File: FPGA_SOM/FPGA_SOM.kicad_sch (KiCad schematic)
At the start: 64 parts, among them J1 Conn_01x14, J2 Conn_01x09, J3 Conn_01x11, J4 Conn_01x04, J5 Conn_01x02, J6 Conn_02x04_Counter_Clockwise, U1 ICE40UP5K-SG48ITR, U101 W25X20CLSN, U2 AP2127N-3.3, U3 AP2127N-1.2, X101 ECS-2520MV-xxx-xx

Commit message: Saving progress.
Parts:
- removed D1: 1N4004, Diode_SMD:D_0603_1608Metric, symbol Diode:1N4004
- removed D102: LED, Diode_SMD:D_0603_1608Metric, symbol Device:LED
- removed J1: Conn_01x14, Connector_PinHeader_2.54mm:PinHeader_1x14_P2.54mm_Vertical, symbol Connector_Generic:Conn_01x14
- removed J2: Conn_01x09, Connector_PinHeader_2.54mm:PinHeader_1x09_P2.54mm_Vertical, symbol Connector_Generic:Conn_01x09
- removed J3: Conn_01x11, Connector_PinHeader_2.54mm:PinHeader_1x11_P2.54mm_Vertical, symbol Connector_Generic:Conn_01x11
- removed J4: Conn_01x04, Connector_PinHeader_2.54mm:PinHeader_1x04_P2.54mm_Vertical, symbol Connector_Generic:Conn_01x04
- removed J6: Conn_02x04_Counter_Clockwise, Connector_PinHeader_2.54mm:PinHeader_2x04_P2.54mm_Vertical, symbol Connector_Generic:Conn_02x04_Counter_Clockwise
- removed R102: 10k, Resistor_SMD:R_0603_1608Metric, symbol Device:R
- removed R103 (x2): 0, Resistor_SMD:R_0603_1608Metric, symbol Device:R
- removed R111, R3, R4, R5: 1k, Resistor_SMD:R_0603_1608Metric, symbol Device:R
- removed TP2: TestPoint, TestPoint:TestPoint_Pad_2.0x2.0mm, symbol Connector:TestPoint
- added H1, H2, H3, H4: MountingHole, MountingHole:MountingHole_3.2mm_M3, symbol Mechanical:MountingHole
- added J1: Conn_01x12, Connector_PinHeader_2.54mm:PinHeader_1x12_P2.54mm_Vertical, symbol Connector_Generic:Conn_01x12
- added J2: Conn_02x05_Counter_Clockwise, Connector_PinHeader_2.54mm:PinHeader_2x05_P2.54mm_Vertical, symbol Connector_Generic:Conn_02x05_Counter_Clockwise
- added J3: Conn_01x06, Connector_PinHeader_2.54mm:PinHeader_1x06_P2.54mm_Vertical, symbol Connector_Generic:Conn_01x06
- added J7: Conn_01x09, Connector_PinHeader_2.54mm:PinHeader_1x09_P2.54mm_Vertical, symbol Connector_Generic:Conn_01x09
- added J8: Conn_01x10, Connector_PinHeader_2.54mm:PinHeader_1x10_P2.54mm_Vertical, symbol Connector_Generic:Conn_01x10
- added R102 (x2), R103 (x2): 10k, Resistor_SMD:R_0603_1608Metric, symbol Device:R
- added R103 (x2): 0, Resistor_SMD:R_0603_1608Metric, symbol Device:R
- C122: value 10u -> 4.7u; footprint Capacitor_SMD:C_0805_2012Metric -> Capacitor_SMD:C_0603_1608Metric
- C137: value 22u -> 10u
- TP1: value TestPoint -> VPLL
- TP10: value TestPoint -> ~{RST}
- TP11: value TestPoint -> CDN
- TP12: value TestPoint -> OSC
- TP3: value TestPoint -> 3V3
- TP4: value TestPoint -> 1V2
- TP5: value TestPoint -> FSS
- TP6: value TestPoint -> ISS
- TP7: value TestPoint -> SCK
- TP8: value TestPoint -> SDO
- TP9: value TestPoint -> SDI
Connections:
- net +5V: now also J1.12 (Pin_12)
- net 3V3: now also U1.24 (VPP_2V5), J1.11 (Pin_11), J2.8 (Pin_8), R102.1, R102.1, R103.1, R103.1
- net CDONE: now also J2.9 (Pin_9), J8.5 (Pin_5)
- net CRESET: now also J2.10 (Pin_10), J8.6 (Pin_6), R102.2
- net FLASH_SS: now also J2.1 (Pin_1)
- net GND: now also J1.10 (Pin_10), J2.7 (Pin_7)
- net ICE_SS: now also R103.2
- net SCK: now also J2.4 (Pin_4), R103.2
- net VCCPLL: now also TP1.1
- net RGB0: now reaches D2.1 (K)
- net RGB0: now also U1.39 (RGB0)
- net V_OSC: now reaches C134.1, C138.1, C143.2, FB1.2, X101.1 (Tri-State), X101.4 (VDD)
- net 20: now reaches U1.20 (IOB_25b_G3)
- net 20: now also J3.4 (Pin_4)
- net 21: now reaches U1.21 (IOB_23b)
- net 21: now also J3.5 (Pin_5)
- net 6: now reaches U1.6 (IOB_13b)
- net 6: now also J8.4 (Pin_4)
- net 9: now reaches U1.9 (IOB_16a)
- net 9: now also J8.7 (Pin_7)
- net 10: now reaches U1.10 (IOB_18a)
- net 10: now also J8.8 (Pin_8)
- net 11: now reaches U1.11 (IOB_20a)
- net 11: now also J8.9 (Pin_9)
- net 12: now reaches U1.12 (IOB_22a)
- net 12: now also J8.10 (Pin_10)
- net 13: now reaches U1.13 (IOB_24a)
- net 13: now also J3.1 (Pin_1)
- net 18: now reaches U1.18 (IOB_31b)
- net 18: now also J3.2 (Pin_2)
- net 19: now reaches U1.19 (IOB_29b)
- net 19: now also J3.3 (Pin_3)
- net RGB2: now reaches D4.1 (K)
- net RGB2: now also U1.41 (RGB2)
- net 23: now reaches U1.23 (IOT_37a)
- net 23: now also J3.6 (Pin_6)
- net 25: now reaches U1.25 (IOT_36b)
- net 25: now also J7.1 (Pin_1)
- net 26: now reaches U1.26 (IOT_39a)
- net 26: now also J7.2 (Pin_2)
- net 27: now reaches U1.27 (IOT_38b)
- net 27: now also J7.3 (Pin_3)
- net 28: now reaches U1.28 (IOT_41a)
- net 28: now also J7.4 (Pin_4)
- net RDP_N: now reaches U1.31 (IOT_42b)
- net RDP_N: now also J7.5 (Pin_5)
- net RDP_P: now reaches U1.32 (IOT_43a)
- net RDP_P: now also J7.6 (Pin_6)
- net 34: now reaches U1.34 (IOT_44b)
- net 34: now also J7.7 (Pin_7)
- net 35_G0: now reaches U1.35 (IOT_46b_G0)
- net 35_G0: now also J7.8 (Pin_8)
- net 36: now reaches U1.36 (IOT_48b)
- net 36: now also J7.9 (Pin_9)
- net 37_G1: now reaches U1.37 (IOT_45a_G1)
- net 37_G1: now also J1.1 (Pin_1)
- net 38: now reaches U1.38 (IOT_50b)
- net 38: now also J1.2 (Pin_2)
- net RGB1: now reaches U1.40 (RGB1)
- net RGB1: now also D3.1 (K)
- net 42: now reaches U1.42 (IOT_51a)
- net 42: now also J1.3 (Pin_3)
- net 43: now reaches U1.43 (IOT_49a)
- net 43: now also J1.4 (Pin_4)
- net 45: now reaches U1.45 (IOB_5b)
- net 45: now also J1.6 (Pin_6)
- net DP1_N: now reaches U1.46 (IOB_0a)
- net DP1_N: now also J1.7 (Pin_7)
- net DP1_P: now reaches U1.47 (IOB_2a)
- net DP1_P: now also J1.8 (Pin_8)
- net 48: now reaches U1.48 (IOB_4a)
- net 48: now also J1.9 (Pin_9)
- net 2: now reaches U1.2 (IOB_6a)
- net 2: now also J8.1 (Pin_1)
- net 3: now reaches U1.3 (IOB_9b)
- net 3: now also J8.2 (Pin_2)
- net 4: now reaches U1.4 (IOB_8a)
- net 4: now also J8.3 (Pin_3)
- net at R102.2, U101.3 (~{WP}): no longer U101.7 (~{HOLD})
- net FLASH_MISO renamed FLASH_DO
- net FLASH_DO: now also J2.2 (Pin_2), R103.1; no longer U1.17 (IOB_33b_SPI_SI)
- net FLASH_MOSI renamed FLASH_DI
- net FLASH_DI: now also J2.3 (Pin_3), R103.1; no longer U1.14 (IOB_32a_SPI_SO)
- net FPGA_OSCILLATOR renamed CLK_IN_G6
- net CLK_IN_G6: now also J1.5 (Pin_5)
- new net: R103.2, U1.17 (IOB_33b_SPI_SI)
- new net: R103.2, U1.14 (IOB_32a_SPI_SO)
- new net: R102.2, U101.7 (~{HOLD})
- no-connect marks 0 -> 2
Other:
- note added: "10-pin IDC Programming Header"
- note added: "1V2 Power supply"
- note added: "3V3 Power supply"
- note added: "Bottom Header"
- note added: "CMOS Crystal oscillator 50 MHz"
- note added: "Don't need resistors as FPGA has programmable current sinks"
- note added: "FPGA Banks and CDONE Indicator LED"
- note added: "Idea of header locations"
- note added: "Left Header"
- note added: "Mounting holes"
- note added: "Non-IO FPGA Power Only need 2.5V if programming NVCM"
- note added: "Pin 30"
- note added: "Pin 5"
- note added: "Right Header"
- note added: "Top Header"
- note added: "VPLL Filtering"
- note added: "between flash and FPGA"
- note added: "between input and flash"
- note removed: "3V3 FPGA decoupling capacitors"
- note removed: "Crystal oscillator for FPGA"
- note removed: "Power supply 3V3, 1V2 and PLL power supply filter"
- note removed: "SPI and I2C pins are not preassigned. I3C pins are:"
- moved on the sheet: C101, C104, C119, C122, C125, C126, C131, C133, C134, C137, C138, C143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

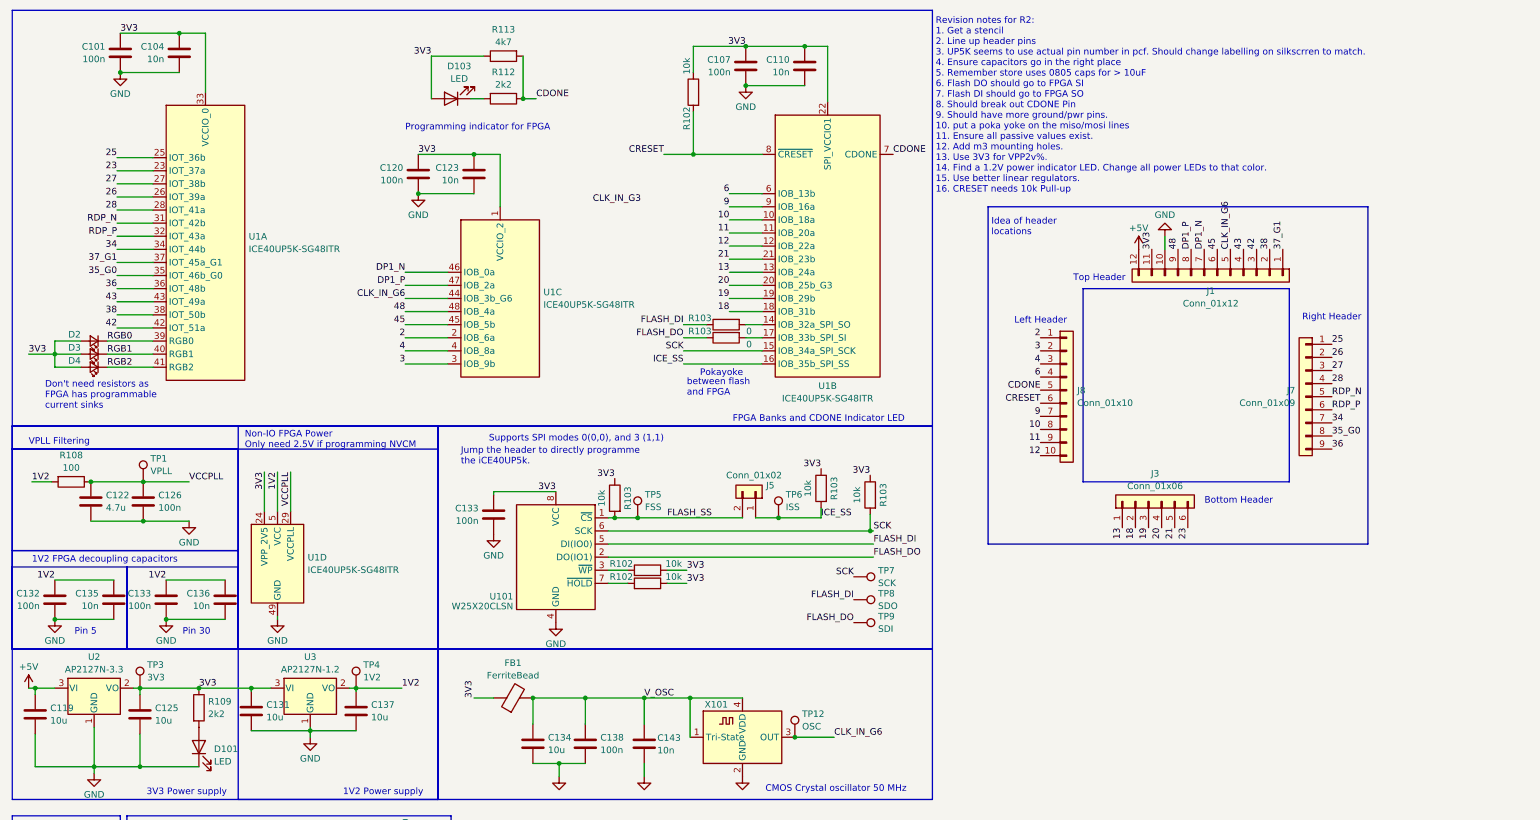
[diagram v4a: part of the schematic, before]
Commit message: Remove some unnecessary capacitors and resize others.
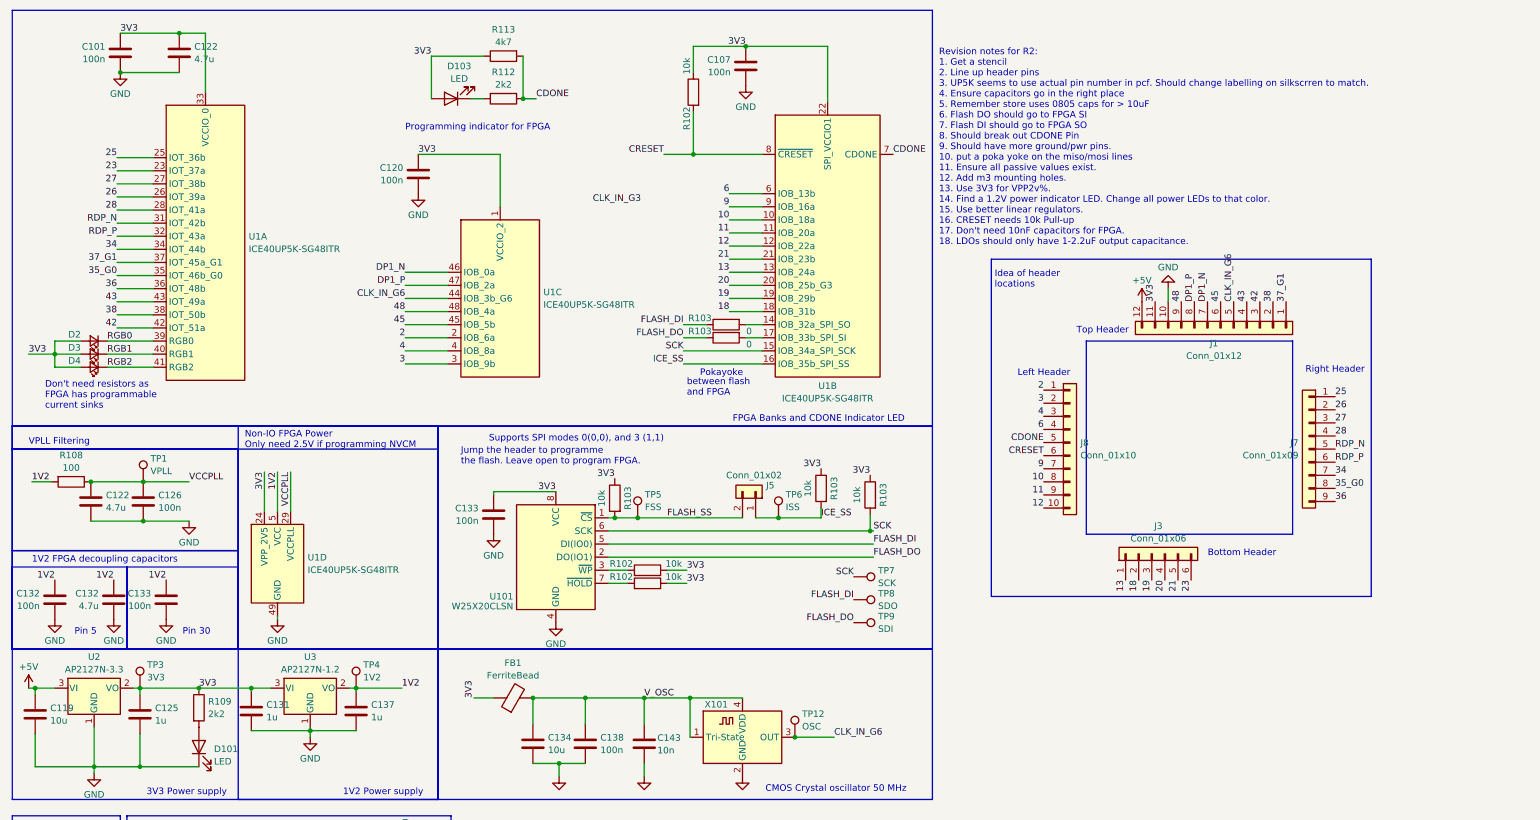
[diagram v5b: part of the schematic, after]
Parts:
- removed C104, C110, C123, C135, C136: 10n, Capacitor_SMD:C_0603_1608Metric, symbol Device:C
- added C122, C132: 4.7u, Capacitor_SMD:C_0603_1608Metric, symbol Device:C
- C125, C131, C137: value 10u -> 1u; footprint Capacitor_SMD:C_0805_2012Metric -> Capacitor_SMD:C_0603_1608Metric
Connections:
- net 1V2: now also C132.1
- net 3V3: now also C122.1
- net GND: now also C122.2, C132.2
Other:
- note added: "Jump the header to programme the flash. Leave open to program FPGA."
- note removed: "Jump the header to directly programme the iCE40UP5k."
- moved on the sheet: J1, J3, J7, J8

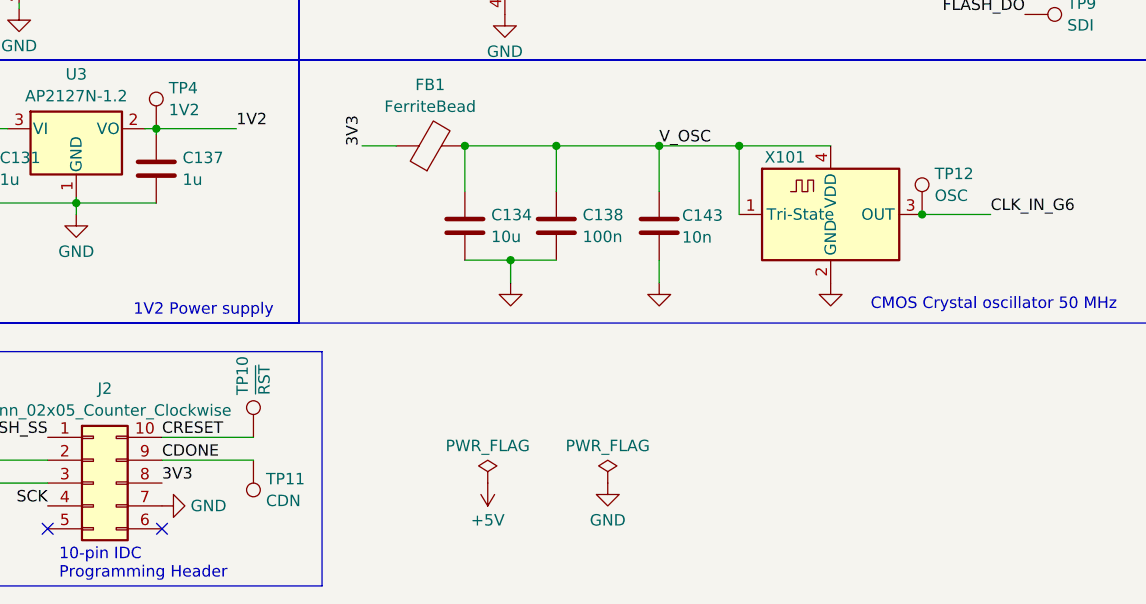
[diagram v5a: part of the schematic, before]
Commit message: Added silkscreen and removed unneded test points.
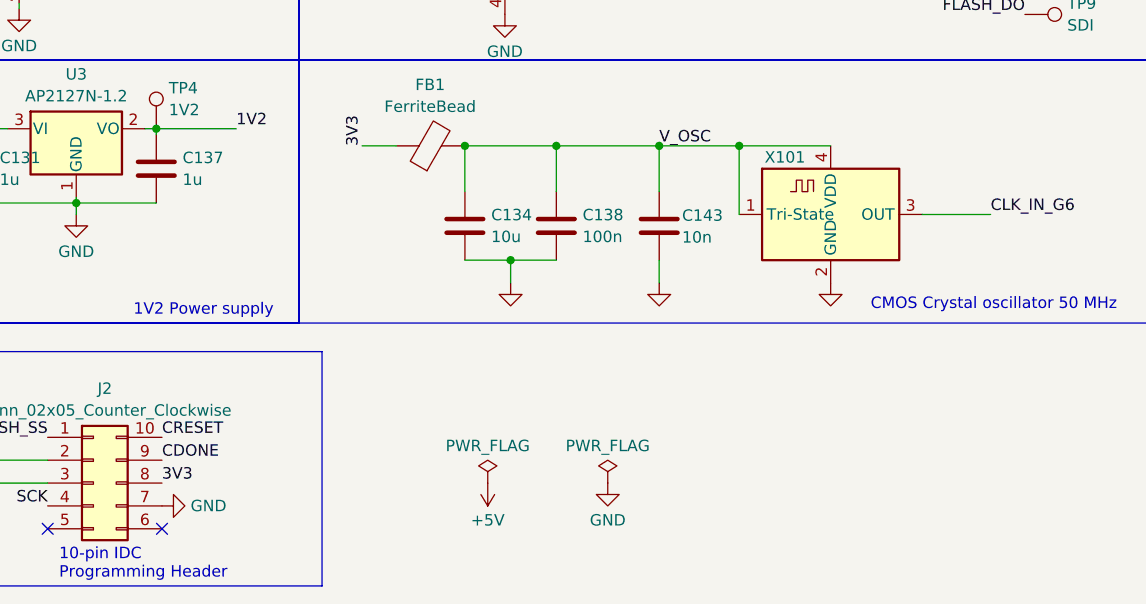
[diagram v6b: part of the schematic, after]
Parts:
- removed TP10: ~{RST}, TestPoint:TestPoint_Pad_2.0x2.0mm, symbol Connector:TestPoint
- removed TP11: CDN, TestPoint:TestPoint_Pad_2.0x2.0mm, symbol Connector:TestPoint
- removed TP12: OSC, TestPoint:TestPoint_Pad_2.0x2.0mm, symbol Connector:TestPoint
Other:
- company: (none) -> Tobias McKellar
- title: (none) -> FPGA System on Module
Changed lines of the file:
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@@
 (kicad_sch (version 20230121) (generator eeschema)
   (paper "A4")
+  (title_block
+    (title "FPGA System on Module")
+    (rev "2")
+    (company "Tobias McKellar")
+  )
   (junction (at 38.735 104.14) (diameter 0) (color 0 0 0 0)
   )
@@
   )
   (junction (at 130.175 111.125) (diameter 0) (color 0 0 0 0)
-  )
-  (junction (at 165.1 153.67) (diameter 0) (color 0 0 0 0)
   )
   (junction (at 38.735 111.76) (diameter 0) (color 0 0 0 0)
@@
     (stroke (width 0) (type default))
   )
-  (wire (pts (xy 90.805 180.975) (xy 80.645 180.975))
-    (stroke (width 0) (type default))
-  )
   (wire (pts (xy 33.655 53.975) (xy 40.64 53.975))
     (stroke (width 0) (type default))
@@
   )
   (wire (pts (xy 143.51 73.66) (xy 147.955 73.66))
-    (stroke (width 0) (type default))
-  )
-  (wire (pts (xy 90.805 178.435) (xy 80.645 178.435))
     (stroke (width 0) (type default))
   )
@@
     )
   )
-  (symbol (lib_id "Connector:TestPoint") (at 90.805 178.435 0) (unit 1)
-    (in_bom yes) (on_board yes) (dnp no)
-    (property "Reference" "TP10" (at 89.5929 173.736 90)
-      (effects (font (size 1.27 1.27)) (justify left))
-    )
-    (property "Value" "~{RST}" (at 92.0171 173.736 90)
-      (effects (font (size 1.27 1.27)) (justify left))
-    )
-    (property "Footprint" "TestPoint:TestPoint_Pad_2.0x2.0mm" (at 95.885 178.435 0)
-      (effects (font (size 1.27 1.27)) hide)
-    )
-    (property "Datasheet" "~" (at 95.885 178.435 0)
-      (effects (font (size 1.27 1.27)) hide)
-    )
-    (pin "1")
-    (instances
-      (project "FPGA_SOM"
-        (path "/c9513ae4-ec90-4b73-ae24-d135d02c4e68"
-          (reference "TP10") (unit 1)
-        )
-      )
-    )
-  )
   (symbol (lib_id "Connector:TestPoint") (at 176.53 131.445 270) (unit 1)
     (in_bom yes) (on_board yes) (dnp no) (fields_autoplaced)
@@
     )
   )
-  (symbol (lib_id "Connector:TestPoint") (at 165.1 153.67 0) (unit 1)
-    (in_bom yes) (on_board yes) (dnp no) (fields_autoplaced)
-    (property "Reference" "TP12" (at 166.497 149.1559 0)
-      (effects (font (size 1.27 1.27)) (justify left))
-    )
-    (property "Value" "OSC" (at 166.497 151.5801 0)
-      (effects (font (size 1.27 1.27)) (justify left))
-    )
-    (property "Footprint" "TestPoint:TestPoint_Pad_2.0x2.0mm" (at 170.18 153.67 0)
-      (effects (font (size 1.27 1.27)) hide)
-    )
-    (property "Datasheet" "~" (at 170.18 153.67 0)
-      (effects (font (size 1.27 1.27)) hide)
-    )
-    (pin "1")
-    (instances
-      (project "FPGA_SOM"
-        (path "/c9513ae4-ec90-4b73-ae24-d135d02c4e68"
-          (reference "TP12") (unit 1)
-        )
-      )
-    )
-  )
   (symbol (lib_id "Device:C") (at 38.1 149.225 0) (unit 1)
     (in_bom yes) (on_board yes) (dnp no) (fields_autoplaced)
@@
         )
       )
-    )
-  )
-  (symbol (lib_id "Connector:TestPoint") (at 90.805 180.975 180) (unit 1)
-    (in_bom yes) (on_board yes) (dnp no) (fields_autoplaced)
-    (property "Reference" "TP11" (at 92.202 183.0649 0)
-      (effects (font (size 1.27 1.27)) (justify right))
-    )
-    (property "Value" "CDN" (at 92.202 185.4891 0)
-      (effects (font (size 1.27 1.27)) (justify right))
-    )
-    (property "Footprint" "TestPoint:TestPoint_Pad_2.0x2.0mm" (at 85.725 180.975 0)
-      (effects (font (size 1.27 1.27)) hide)
-    )
-    (property "Datasheet" "~" (at 85.725 180.975 0)
-      (effects (font (size 1.27 1.27)) hide)
-    )
-    (pin "1")
-    (instances
-      (project "FPGA_SOM"
-        (path "/c9513ae4-ec90-4b73-ae24-d135d02c4e68"
-          (reference "TP11") (unit 1)
-        )
-      )
